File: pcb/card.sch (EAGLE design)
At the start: 20 parts, among them IC1 74HC14D, IC2 24LC256SN, Q1 BC817

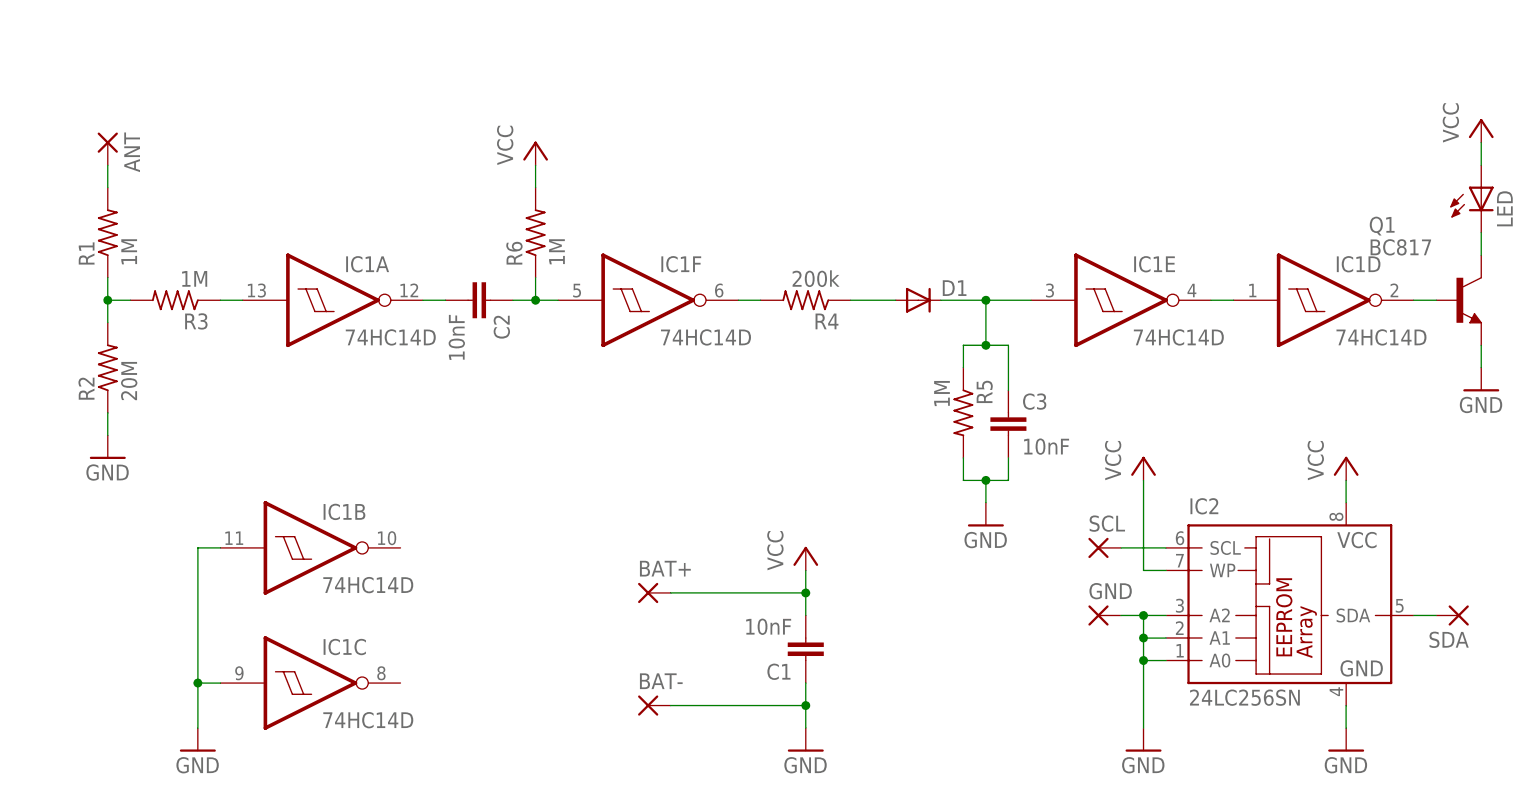
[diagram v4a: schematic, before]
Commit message: Added a bypass cap & improved the layout.
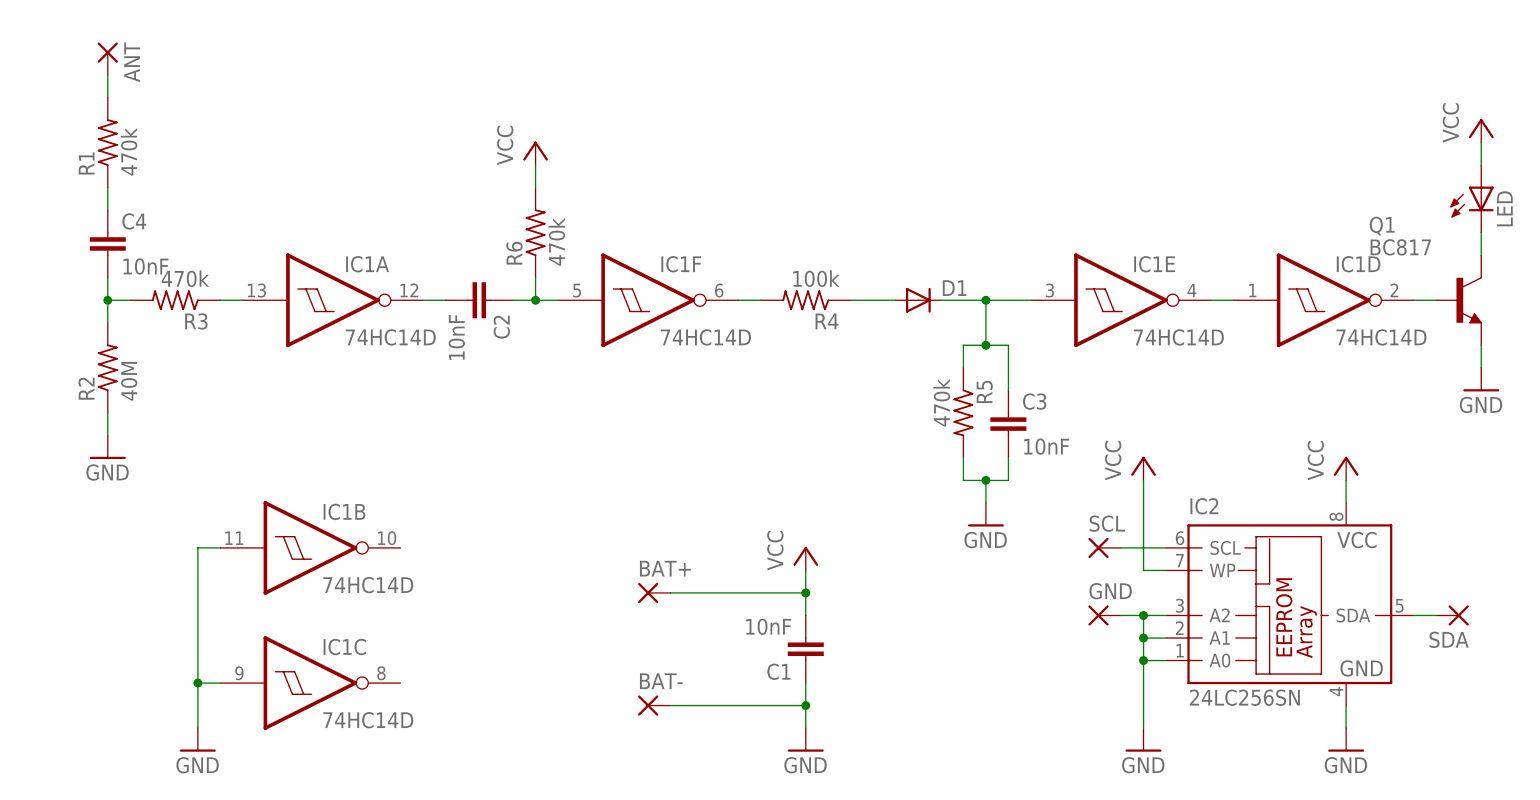
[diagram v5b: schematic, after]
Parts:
- added C4: 10nF, resistor:C-EUC1206K
- R1, R3, R5, R6: value 1M -> 470k
- R2: value 20M -> 40M
- R4: value 200k -> 100k
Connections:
- new net N$1: C4.1, R1.1
- net N$2: now also C4.2; no longer R1.1
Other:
- moved on the sheet: ANT, R1
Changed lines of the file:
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@@
 <grid distance="0.1" unitdist="inch" unit="inch" style="lines" multiple="1" display="no" altdistance="0.01" altunitdist="inch" altunit="inch"/>
 <layers>
-<layer number="1" name="Top" color="4" fill="1" visible="yes" active="no"/>
-<layer number="16" name="Bottom" color="1" fill="1" visible="yes" active="no"/>
-<layer number="17" name="Pads" color="2" fill="1" visible="yes" active="no"/>
-<layer number="18" name="Vias" color="2" fill="1" visible="yes" active="no"/>
-<layer number="19" name="Unrouted" color="6" fill="1" visible="yes" active="no"/>
-<layer number="20" name="Dimension" color="15" fill="1" visible="yes" active="no"/>
-<layer number="21" name="tPlace" color="7" fill="1" visible="yes" active="no"/>
-<layer number="22" name="bPlace" color="7" fill="1" visible="yes" active="no"/>
-<layer number="23" name="tOrigins" color="15" fill="1" visible="yes" active="no"/>
-<layer number="24" name="bOrigins" color="15" fill="1" visible="yes" active="no"/>
-<layer number="25" name="tNames" color="7" fill="1" visible="yes" active="no"/>
-<layer number="26" name="bNames" color="7" fill="1" visible="yes" active="no"/>
-<layer number="27" name="tValues" color="7" fill="1" visible="yes" active="no"/>
-<layer number="28" name="bValues" color="7" fill="1" visible="yes" active="no"/>
+<layer number="1" name="Top" color="4" fill="1" visible="no" active="no"/>
+<layer number="16" name="Bottom" color="1" fill="1" visible="no" active="no"/>
+<layer number="17" name="Pads" color="2" fill="1" visible="no" active="no"/>
+<layer number="18" name="Vias" color="2" fill="1" visible="no" active="no"/>
+<layer number="19" name="Unrouted" color="6" fill="1" visible="no" active="no"/>
+<layer number="20" name="Dimension" color="15" fill="1" visible="no" active="no"/>
+<layer number="21" name="tPlace" color="7" fill="1" visible="no" active="no"/>
+<layer number="22" name="bPlace" color="7" fill="1" visible="no" active="no"/>
+<layer number="23" name="tOrigins" color="15" fill="1" visible="no" active="no"/>
+<layer number="24" name="bOrigins" color="15" fill="1" visible="no" active="no"/>
+<layer number="25" name="tNames" color="7" fill="1" visible="no" active="no"/>
+<layer number="26" name="bNames" color="7" fill="1" visible="no" active="no"/>
+<layer number="27" name="tValues" color="7" fill="1" visible="no" active="no"/>
+<layer number="28" name="bValues" color="7" fill="1" visible="no" active="no"/>
 <layer number="29" name="tStop" color="7" fill="3" visible="no" active="no"/>
 <layer number="30" name="bStop" color="7" fill="6" visible="no" active="no"/>
@@
 <layer number="35" name="tGlue" color="7" fill="4" visible="no" active="no"/>
 <layer number="36" name="bGlue" color="7" fill="5" visible="no" active="no"/>
-<layer number="37" name="tTest" color="7" fill="1" visible="yes" active="no"/>
-<layer number="38" name="bTest" color="7" fill="1" visible="yes" active="no"/>
+<layer number="37" name="tTest" color="7" fill="1" visible="no" active="no"/>
+<layer number="38" name="bTest" color="7" fill="1" visible="no" active="no"/>
 <layer number="39" name="tKeepout" color="4" fill="11" visible="no" active="no"/>
 <layer number="40" name="bKeepout" color="1" fill="11" visible="no" active="no"/>
@@
 <layer number="44" name="Drills" color="7" fill="1" visible="no" active="no"/>
 <layer number="45" name="Holes" color="7" fill="1" visible="no" active="no"/>
-<layer number="46" name="Milling" color="3" fill="1" visible="yes" active="no"/>
-<layer number="47" name="Measures" color="7" fill="1" visible="yes" active="no"/>
-<layer number="48" name="Document" color="7" fill="1" visible="yes" active="no"/>
-<layer number="49" name="Reference" color="7" fill="1" visible="yes" active="no"/>
-<layer number="51" name="tDocu" color="7" fill="1" visible="yes" active="no"/>
-<layer number="52" name="bDocu" color="7" fill="1" visible="yes" active="no"/>
+<layer number="46" name="Milling" color="3" fill="1" visible="no" active="no"/>
+<layer number="47" name="Measures" color="7" fill="1" visible="no" active="no"/>
+<layer number="48" name="Document" color="7" fill="1" visible="no" active="no"/>
+<layer number="49" name="Reference" color="7" fill="1" visible="no" active="no"/>
+<layer number="51" name="tDocu" color="7" fill="1" visible="no" active="no"/>
+<layer number="52" name="bDocu" color="7" fill="1" visible="no" active="no"/>
 <layer number="90" name="Modules" color="5" fill="1" visible="yes" active="yes"/>
 <layer number="91" name="Nets" color="2" fill="1" visible="yes" active="yes"/>
@@
 <part name="P+2" library="supply1" deviceset="VCC" device=""/>
 <part name="P+3" library="supply1" deviceset="VCC" device=""/>
-<part name="R1" library="resistor" deviceset="R-US_" device="M1206" value="1M"/>
-<part name="R2" library="resistor" deviceset="R-US_" device="M1206" value="20M"/>
-<part name="R3" library="resistor" deviceset="R-US_" device="M1206" value="1M"/>
-<part name="R4" library="resistor" deviceset="R-US_" device="M1206" value="200k"/>
-<part name="R5" library="resistor" deviceset="R-US_" device="M1206" value="1M"/>
+<part name="R1" library="resistor" deviceset="R-US_" device="M1206" value="470k"/>
+<part name="R2" library="resistor" deviceset="R-US_" device="M1206" value="40M"/>
+<part name="R3" library="resistor" deviceset="R-US_" device="M1206" value="470k"/>
+<part name="R4" library="resistor" deviceset="R-US_" device="M1206" value="100k"/>
+<part name="R5" library="resistor" deviceset="R-US_" device="M1206" value="470k"/>
 <part name="GND1" library="supply1" deviceset="GND" device=""/>
 <part name="GND2" library="supply1" deviceset="GND" device=""/>
@@
 <part name="Q1" library="transistor" deviceset="*-NPN-" device="SOT23-BEC" technology="BC817-16" value="BC817"/>
 <part name="LED" library="led" deviceset="LED" device="CHIPLED_1206"/>
-<part name="R6" library="resistor" deviceset="R-US_" device="M1206" value="1M"/>
+<part name="R6" library="resistor" deviceset="R-US_" device="M1206" value="470k"/>
 <part name="C1" library="resistor" deviceset="C-EU" device="C1206K" value="10nF"/>
 <part name="C2" library="resistor" deviceset="C-EU" device="C1206K" value="10nF"/>
@@
 <part name="IC2" library="microchip" deviceset="24*" device="SN" technology="LC256"/>
 <part name="GND" library="wirepad" deviceset="SMD2" device=""/>
+<part name="C4" library="resistor" deviceset="C-EU" device="C1206K" value="10nF"/>
 </parts>
 <sheets>
@@
 <instance part="P+2" gate="VCC" x="30.48" y="68.58"/>
 <instance part="P+3" gate="VCC" x="137.16" y="71.12"/>
-<instance part="R1" gate="G$1" x="-17.78" y="58.42" rot="R90"/>
+<instance part="R1" gate="G$1" x="-17.78" y="68.58" rot="R90"/>
 <instance part="R2" gate="G$1" x="-17.78" y="43.18" rot="R90"/>
 <instance part="R3" gate="G$1" x="-10.16" y="50.8" rot="R180"/>
@@
 <instance part="BAT+" gate="1" x="43.18" y="17.78"/>
 <instance part="BAT-" gate="1" x="43.18" y="5.08"/>
-<instance part="ANT" gate="1" x="-17.78" y="68.58" rot="R270"/>
+<instance part="ANT" gate="1" x="-17.78" y="78.74" rot="R270"/>
 <instance part="IC2" gate="G$1" x="114.3" y="15.24"/>
 <instance part="GND" gate="1" x="93.98" y="15.24"/>
+<instance part="C4" gate="G$1" x="-17.78" y="58.42"/>
 </instances>
 <busses>
@@
 <segment>
 <pinref part="R1" gate="G$1" pin="2"/>
-<wire x1="-17.78" y1="66.04" x2="-17.78" y2="63.5" width="0.1524" layer="91"/>
+<wire x1="-17.78" y1="76.2" x2="-17.78" y2="73.66" width="0.1524" layer="91"/>
 <pinref part="ANT" gate="1" pin="P"/>
 </segment>
@@
 <net name="N$2" class="0">
 <segment>
-<pinref part="R1" gate="G$1" pin="1"/>
 <pinref part="R2" gate="G$1" pin="2"/>
-<wire x1="-17.78" y1="53.34" x2="-17.78" y2="50.8" width="0.1524" layer="91"/>
 <pinref part="R3" gate="G$1" pin="2"/>
 <wire x1="-17.78" y1="50.8" x2="-17.78" y2="48.26" width="0.1524" layer="91"/>
 <wire x1="-15.24" y1="50.8" x2="-17.78" y2="50.8" width="0.1524" layer="91"/>
+<pinref part="C4" gate="G$1" pin="2"/>
+<wire x1="-17.78" y1="53.34" x2="-17.78" y2="50.8" width="0.1524" layer="91"/>
 <junction x="-17.78" y="50.8"/>
 </segment>
@@
 </segment>
 </net>
+<net name="N$1" class="0">
+<segment>
+<pinref part="R1" gate="G$1" pin="1"/>
+<pinref part="C4" gate="G$1" pin="1"/>
+<wire x1="-17.78" y1="63.5" x2="-17.78" y2="60.96" width="0.1524" layer="91"/>
+</segment>
+</net>

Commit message: Apparently 10M Ohm is as high as it gets for reasonable amount of money.
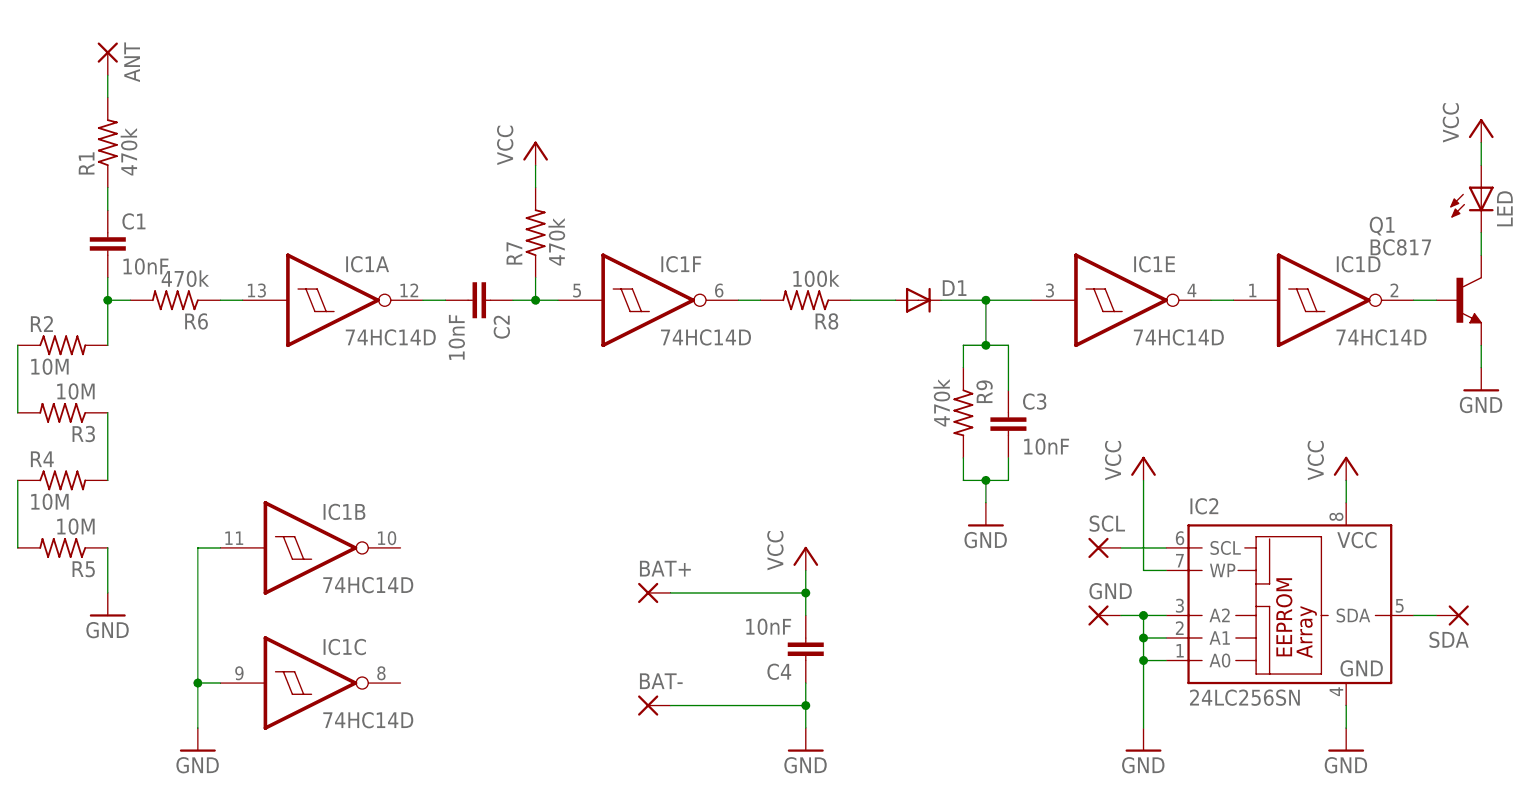
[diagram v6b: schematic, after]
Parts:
- added R7, R9: 470k, resistor:R-US_M1206
- added R8: 100k, resistor:R-US_M1206
- R2: value 40M -> 10M
- R3, R5: value 470k -> 10M
- R4: value 100k -> 10M
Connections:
- new net N$14: R2.1, R3.2
- new net N$15: R3.1, R4.2
- new net N$16: R4.1, R5.2
- net GND: now also C4.1, R5.1, R9.2; no longer C1.1, R2.1, R5.2
- net N$1: now also C1.1; no longer C4.1
- net N$2: now also C1.2, R6.2; no longer C4.2, R3.2
- net N$3: now also R6.1; no longer R3.1
- net N$5: now also R7.1; no longer R6.1
- net N$6: now also R8.2; no longer R4.2
- net N$7: now also R8.1; no longer R4.1
- net N$8: now also R9.1; no longer R5.1
- net VCC: now also C4.2, R7.2; no longer C1.2, R6.2
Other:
- moved on the sheet: C1, C4, R2, R3, R4, R5, R6

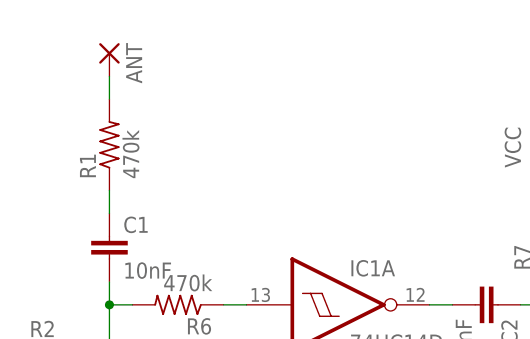
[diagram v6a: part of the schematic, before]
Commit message: Improved the antenna.
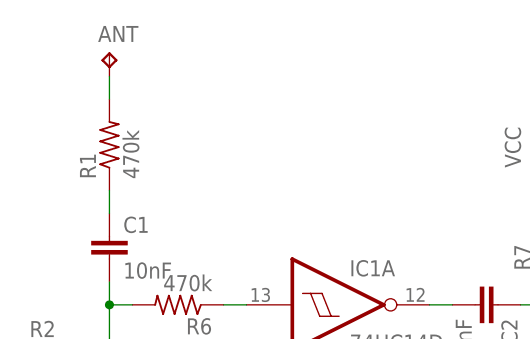
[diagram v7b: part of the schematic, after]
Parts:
- ANT: value (none) -> TPB1,27; device wirepad:SMD2 -> testpad:TPB1,27
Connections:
- net ANT: now also ANT.TP; no longer ANT.P
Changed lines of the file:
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@@
 <part name="BAT+" library="wirepad" deviceset="SMD2" device=""/>
 <part name="BAT-" library="wirepad" deviceset="SMD2" device=""/>
-<part name="ANT" library="wirepad" deviceset="SMD2" device=""/>
 <part name="IC2" library="microchip" deviceset="24*" device="SN" technology="LC256"/>
 <part name="GND" library="wirepad" deviceset="SMD2" device=""/>
@@
 <part name="R4" library="resistor" deviceset="R-US_" device="M1206" value="10M"/>
 <part name="R5" library="resistor" deviceset="R-US_" device="M1206" value="10M"/>
+<part name="ANT" library="testpad" deviceset="TP" device="B1,27"/>
 </parts>
 <sheets>
@@
 <instance part="BAT+" gate="1" x="43.18" y="17.78"/>
 <instance part="BAT-" gate="1" x="43.18" y="5.08"/>
-<instance part="ANT" gate="1" x="-17.78" y="78.74" rot="R270"/>
 <instance part="IC2" gate="G$1" x="114.3" y="15.24"/>
 <instance part="GND" gate="1" x="93.98" y="15.24"/>
@@
 <instance part="R4" gate="G$1" x="-22.86" y="30.48"/>
 <instance part="R5" gate="G$1" x="-22.86" y="22.86" rot="R180"/>
+<instance part="ANT" gate="G$1" x="-17.78" y="78.74"/>
 </instances>
 <busses>
@@
 <pinref part="R1" gate="G$1" pin="2"/>
 <wire x1="-17.78" y1="76.2" x2="-17.78" y2="73.66" width="0.1524" layer="91"/>
-<pinref part="ANT" gate="1" pin="P"/>
+<pinref part="ANT" gate="G$1" pin="TP"/>
 </segment>
 </net>
